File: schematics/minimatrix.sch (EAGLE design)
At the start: 9 parts

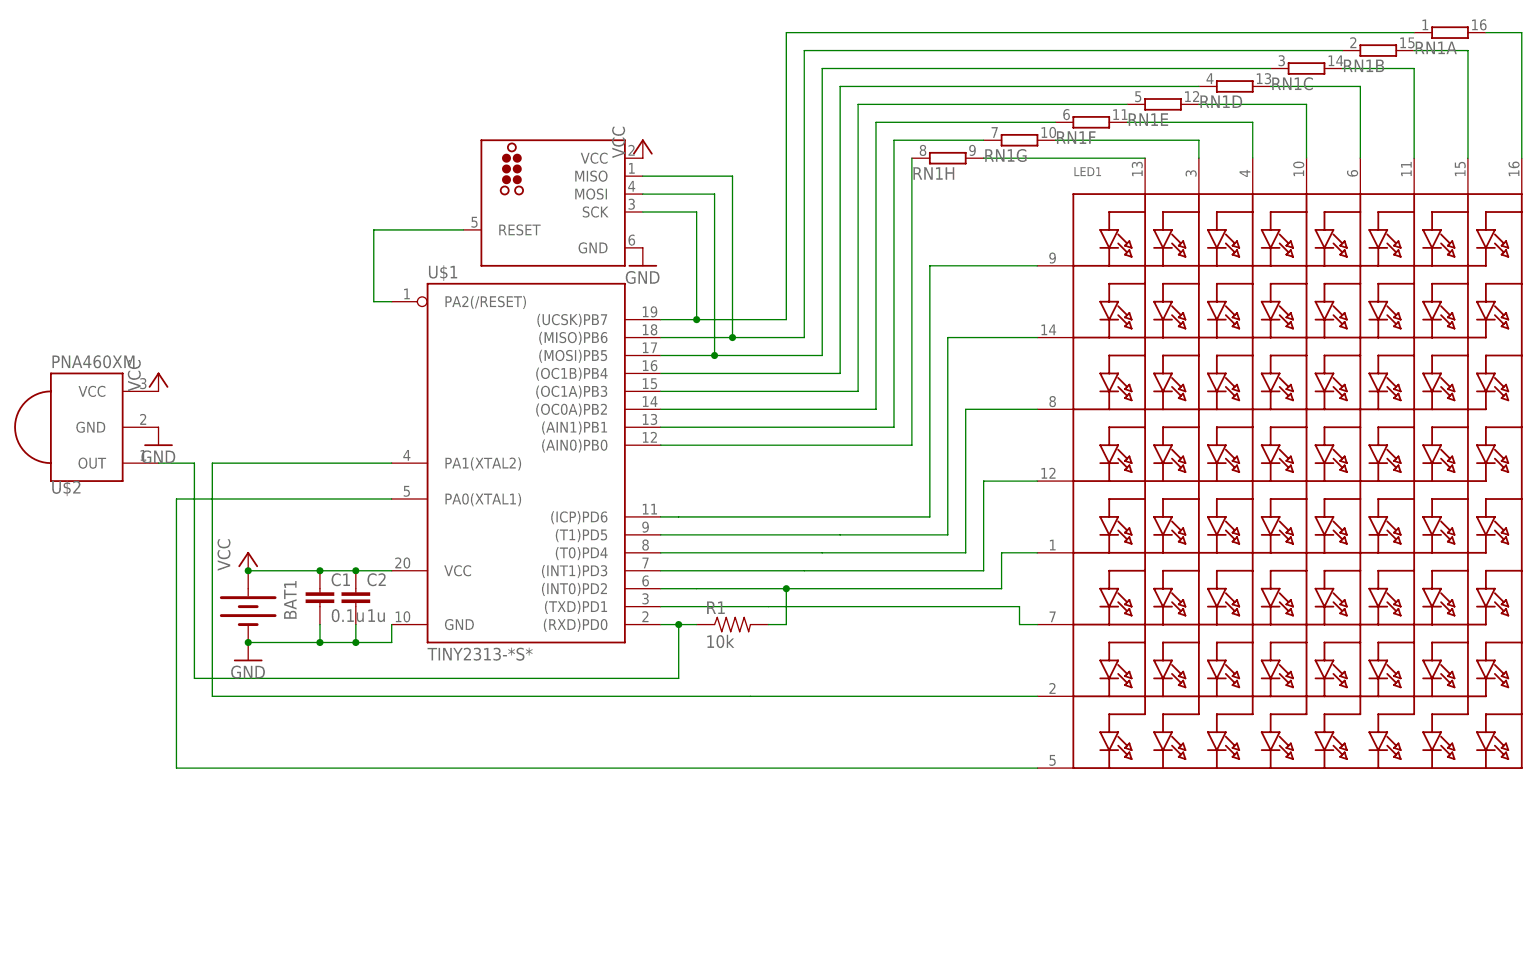
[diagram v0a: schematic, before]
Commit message: Update design restoring IR receiver.
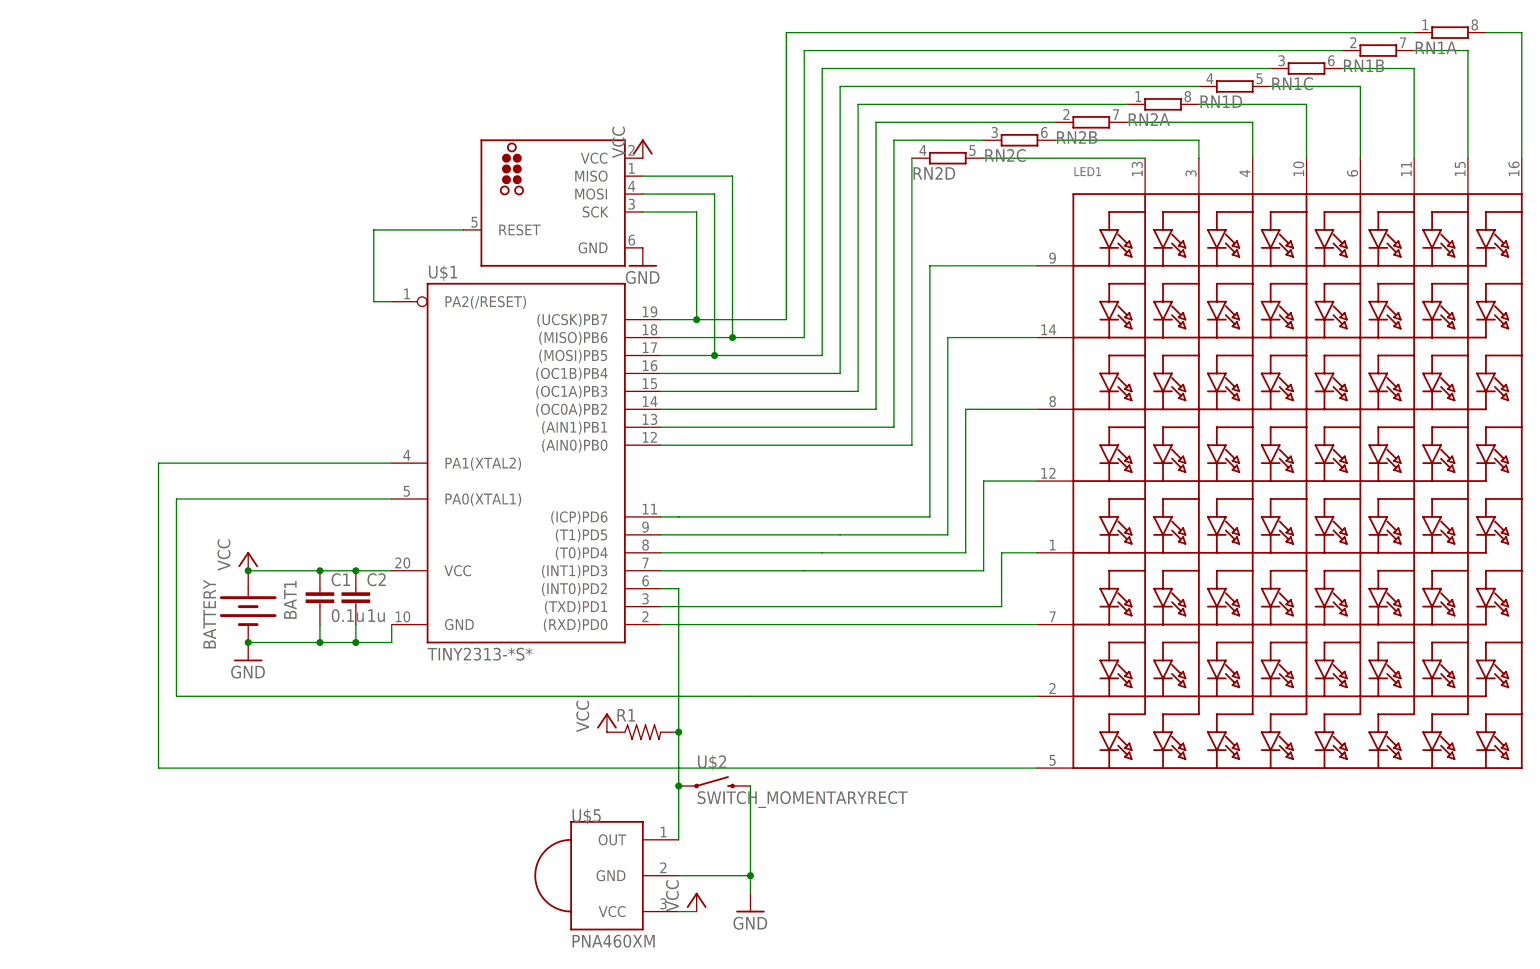
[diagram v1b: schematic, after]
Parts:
- added RN2: (no value), resistor-dil:4R-NCAY16
- added U$5: PNA460XM, adafruit:PNA460XM
- BAT1: value (none) -> BATTERY; device SparkFun-Electromechanical:BATTERY20MM_4LEGS -> nickparts:BATTERY
- R1: value 10k -> (none)
- RN1: device resistor-dil:8R-NEXB2HV -> resistor-dil:4R-NCAY16
- U$2: value PNA460XM -> SWITCH_MOMENTARYRECT; device adafruit:PNA460XM -> nickparts:SWITCH_MOMENTARYRECT
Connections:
- removed net R6: LED1.K6, U$1.(TXD)PD1
- removed net R8: LED1.K8, U$1.PA0(XTAL1)
- removed net ROW5: U$1.PA1(XTAL2)
- new net N$12: LED1.K8, U$1.PA1(XTAL2)
- new net N$13: R1.2, U$1.(INT0)PD2, U$2.1, U$5.OUT
- net C1: now also RN2D.1; no longer RN1H.1
- net C2: now also RN2C.1; no longer RN1G.1
- net C3: now also RN2B.1; no longer RN1F.1
- net C4: now also RN2A.1; no longer RN1E.1
- net GND: now also U$2.2, U$5.GND; no longer U$2.GND
- net N$1: now also LED1.K6; no longer R1.1, U$2.OUT
- net N$10: now also RN2D.2; no longer RN1H.2
- net N$11: now also U$1.(TXD)PD1; no longer R1.2, U$1.(INT0)PD2
- net N$3: now also RN2C.2; no longer RN1G.2
- net N$4: now also RN2B.2; no longer RN1F.2
- net N$5: now also RN2A.2; no longer RN1E.2
- net R7: now also U$1.PA0(XTAL1)
- net VCC: now also R1.1, U$5.VCC; no longer U$2.VCC
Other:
- moved on the sheet: R1, RN1A, RN1B, RN1C, RN1D

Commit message: Tweaks for production version
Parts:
- renumbered U$1 to IC1, U$2 to SW1, U$5 to IC2
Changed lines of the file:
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@@
 <parts>
 <part name="LED1" library="adafruit" deviceset="SEGMENT_8X8_ROWCATHODE" device="M12A881UR"/>
-<part name="U$1" library="avr-7" deviceset="TINY2313*" device="-*S*"/>
+<part name="IC1" library="avr-7" deviceset="TINY2313*" device="-*S*"/>
 <part name="BAT1" library="nickparts" deviceset="BATTERY" device=""/>
 <part name="U$3" library="tag-connect" deviceset="TC2030_AVR" device="MCP-NL"/>
@@
 <part name="RN1" library="resistor-dil" deviceset="4R-N" device="CAY16"/>
 <part name="RN2" library="resistor-dil" deviceset="4R-N" device="CAY16"/>
-<part name="U$2" library="nickparts" deviceset="SWITCH_MOMENTARY" device="RECT"/>
+<part name="SW1" library="nickparts" deviceset="SWITCH_MOMENTARY" device="RECT"/>
 <part name="GND3" library="supply1" deviceset="GND" device=""/>
-<part name="U$5" library="adafruit" deviceset="PNA460XM" device=""/>
+<part name="IC2" library="adafruit" deviceset="PNA460XM" device=""/>
 <part name="P+3" library="supply1" deviceset="VCC" device=""/>
 <part name="R1" library="SparkFun-Passives" deviceset="RESISTOR" device="0805-RES"/>
@@
 <instances>
 <instance part="LED1" gate="G$1" x="106.68" y="55.88"/>
-<instance part="U$1" gate="G$1" x="-2.54" y="66.04"/>
+<instance part="IC1" gate="G$1" x="-2.54" y="66.04"/>
 <instance part="BAT1" gate="G$1" x="-43.18" y="40.64" rot="R270"/>
 <instance part="U$3" gate="G$1" x="10.16" y="88.9" rot="MR0"/>
@@
 <instance part="RN2" gate="C" x="66.04" y="106.68"/>
 <instance part="RN2" gate="D" x="55.88" y="104.14"/>
-<instance part="U$2" gate="G$1" x="22.86" y="15.24"/>
+<instance part="SW1" gate="G$1" x="22.86" y="15.24"/>
 <instance part="GND3" gate="1" x="27.94" y="-2.54"/>
-<instance part="U$5" gate="G$1" x="7.62" y="2.54"/>
+<instance part="IC2" gate="G$1" x="7.62" y="2.54"/>
 <instance part="P+3" gate="VCC" x="20.32" y="0"/>
 <instance part="R1" gate="G$1" x="12.7" y="22.86"/>
@@
 <pinref part="BAT1" gate="G$1" pin="+"/>
 <pinref part="P+1" gate="VCC" pin="VCC"/>
-<pinref part="U$1" gate="G$1" pin="VCC"/>
+<pinref part="IC1" gate="G$1" pin="VCC"/>
 <wire x1="-22.86" y1="45.72" x2="-27.94" y2="45.72" width="0.1524" layer="91"/>
 <junction x="-43.18" y="45.72"/>
@@
 </segment>
 <segment>
-<pinref part="U$5" gate="G$1" pin="VCC"/>
+<pinref part="IC2" gate="G$1" pin="VCC"/>
 <pinref part="P+3" gate="VCC" pin="VCC"/>
 <wire x1="20.32" y1="-2.54" x2="17.78" y2="-2.54" width="0.1524" layer="91"/>
@@
 <pinref part="BAT1" gate="G$1" pin="-"/>
 <pinref part="GND2" gate="1" pin="GND"/>
-<pinref part="U$1" gate="G$1" pin="GND"/>
+<pinref part="IC1" gate="G$1" pin="GND"/>
 <wire x1="-43.18" y1="35.56" x2="-33.02" y2="35.56" width="0.1524" layer="91"/>
 <wire x1="-33.02" y1="35.56" x2="-27.94" y2="35.56" width="0.1524" layer="91"/>
@@
 </segment>
 <segment>
-<pinref part="U$2" gate="G$1" pin="2"/>
+<pinref part="SW1" gate="G$1" pin="2"/>
 <pinref part="GND3" gate="1" pin="GND"/>
 <wire x1="27.94" y1="15.24" x2="27.94" y2="2.54" width="0.1524" layer="91"/>
-<pinref part="U$5" gate="G$1" pin="GND"/>
+<pinref part="IC2" gate="G$1" pin="GND"/>
 <wire x1="27.94" y1="2.54" x2="27.94" y2="0" width="0.1524" layer="91"/>
 <wire x1="17.78" y1="2.54" x2="27.94" y2="2.54" width="0.1524" layer="91"/>
@@
 <net name="C8" class="0">
 <segment>
-<pinref part="U$1" gate="G$1" pin="(UCSK)PB7"/>
+<pinref part="IC1" gate="G$1" pin="(UCSK)PB7"/>
 <wire x1="15.24" y1="81.28" x2="20.32" y2="81.28" width="0.1524" layer="91"/>
 <wire x1="20.32" y1="81.28" x2="20.32" y2="96.52" width="0.1524" layer="91"/>
@@
 <net name="N$2" class="0">
 <segment>
-<pinref part="U$1" gate="G$1" pin="PA2(/RESET)"/>
+<pinref part="IC1" gate="G$1" pin="PA2(/RESET)"/>
 <wire x1="-22.86" y1="83.82" x2="-25.4" y2="83.82" width="0.1524" layer="91"/>
 <wire x1="-25.4" y1="83.82" x2="-25.4" y2="93.98" width="0.1524" layer="91"/>
@@
 <wire x1="12.7" y1="99.06" x2="22.86" y2="99.06" width="0.1524" layer="91"/>
 <wire x1="22.86" y1="99.06" x2="22.86" y2="76.2" width="0.1524" layer="91"/>
-<pinref part="U$1" gate="G$1" pin="(MOSI)PB5"/>
+<pinref part="IC1" gate="G$1" pin="(MOSI)PB5"/>
 <wire x1="22.86" y1="76.2" x2="15.24" y2="76.2" width="0.1524" layer="91"/>
 <wire x1="38.1" y1="116.84" x2="38.1" y2="76.2" width="0.1524" layer="91"/>
@@
 <wire x1="12.7" y1="101.6" x2="25.4" y2="101.6" width="0.1524" layer="91"/>
 <wire x1="25.4" y1="101.6" x2="25.4" y2="78.74" width="0.1524" layer="91"/>
-<pinref part="U$1" gate="G$1" pin="(MISO)PB6"/>
+<pinref part="IC1" gate="G$1" pin="(MISO)PB6"/>
 <wire x1="25.4" y1="78.74" x2="15.24" y2="78.74" width="0.1524" layer="91"/>
 <wire x1="35.56" y1="119.38" x2="35.56" y2="78.74" width="0.1524" layer="91"/>
@@
 <wire x1="53.34" y1="88.9" x2="68.58" y2="88.9" width="0.1524" layer="91"/>
 <wire x1="53.34" y1="53.34" x2="17.78" y2="53.34" width="0.1524" layer="91"/>
-<pinref part="U$1" gate="G$1" pin="(ICP)PD6"/>
+<pinref part="IC1" gate="G$1" pin="(ICP)PD6"/>
 <wire x1="17.78" y1="53.34" x2="15.24" y2="53.34" width="0.1524" layer="91"/>
 </segment>
@@
 <net name="R2" class="0">
 <segment>
-<pinref part="U$1" gate="G$1" pin="(T1)PD5"/>
+<pinref part="IC1" gate="G$1" pin="(T1)PD5"/>
 <wire x1="15.24" y1="50.8" x2="40.64" y2="50.8" width="0.1524" layer="91"/>
 <wire x1="55.88" y1="50.8" x2="55.88" y2="78.74" width="0.1524" layer="91"/>
@@
 <net name="R3" class="0">
 <segment>
-<pinref part="U$1" gate="G$1" pin="(T0)PD4"/>
+<pinref part="IC1" gate="G$1" pin="(T0)PD4"/>
 <wire x1="15.24" y1="48.26" x2="38.1" y2="48.26" width="0.1524" layer="91"/>
 <wire x1="58.42" y1="48.26" x2="58.42" y2="68.58" width="0.1524" layer="91"/>
@@
 <net name="R4" class="0">
 <segment>
-<pinref part="U$1" gate="G$1" pin="(INT1)PD3"/>
+<pinref part="IC1" gate="G$1" pin="(INT1)PD3"/>
 <wire x1="15.24" y1="45.72" x2="35.56" y2="45.72" width="0.1524" layer="91"/>
 <wire x1="60.96" y1="45.72" x2="60.96" y2="58.42" width="0.1524" layer="91"/>
@@
 <pinref part="LED1" gate="G$1" pin="K7"/>
 <wire x1="27.94" y1="27.94" x2="68.58" y2="27.94" width="0.1524" layer="91"/>
-<pinref part="U$1" gate="G$1" pin="PA0(XTAL1)"/>
+<pinref part="IC1" gate="G$1" pin="PA0(XTAL1)"/>
 <wire x1="-22.86" y1="55.88" x2="-53.34" y2="55.88" width="0.1524" layer="91"/>
 <wire x1="-53.34" y1="55.88" x2="-53.34" y2="27.94" width="0.1524" layer="91"/>
@@
 <segment>
 <wire x1="50.8" y1="104.14" x2="50.8" y2="63.5" width="0.1524" layer="91"/>
-<pinref part="U$1" gate="G$1" pin="(AIN0)PB0"/>
+<pinref part="IC1" gate="G$1" pin="(AIN0)PB0"/>
 <wire x1="50.8" y1="63.5" x2="15.24" y2="63.5" width="0.1524" layer="91"/>
 <pinref part="RN2" gate="D" pin="1"/>
@@
 <segment>
 <wire x1="48.26" y1="106.68" x2="48.26" y2="66.04" width="0.1524" layer="91"/>
-<pinref part="U$1" gate="G$1" pin="(AIN1)PB1"/>
+<pinref part="IC1" gate="G$1" pin="(AIN1)PB1"/>
 <wire x1="48.26" y1="66.04" x2="15.24" y2="66.04" width="0.1524" layer="91"/>
 <pinref part="RN2" gate="C" pin="1"/>
@@
 <segment>
 <wire x1="45.72" y1="109.22" x2="45.72" y2="68.58" width="0.1524" layer="91"/>
-<pinref part="U$1" gate="G$1" pin="(OC0A)PB2"/>
+<pinref part="IC1" gate="G$1" pin="(OC0A)PB2"/>
 <wire x1="45.72" y1="68.58" x2="15.24" y2="68.58" width="0.1524" layer="91"/>
 <pinref part="RN2" gate="B" pin="1"/>
@@
 <segment>
 <wire x1="43.18" y1="111.76" x2="43.18" y2="71.12" width="0.1524" layer="91"/>
-<pinref part="U$1" gate="G$1" pin="(OC1A)PB3"/>
+<pinref part="IC1" gate="G$1" pin="(OC1A)PB3"/>
 <wire x1="43.18" y1="71.12" x2="15.24" y2="71.12" width="0.1524" layer="91"/>
 <pinref part="RN2" gate="A" pin="1"/>
@@
 <segment>
 <wire x1="40.64" y1="114.3" x2="40.64" y2="73.66" width="0.1524" layer="91"/>
-<pinref part="U$1" gate="G$1" pin="(OC1B)PB4"/>
+<pinref part="IC1" gate="G$1" pin="(OC1B)PB4"/>
 <wire x1="40.64" y1="73.66" x2="15.24" y2="73.66" width="0.1524" layer="91"/>
 <pinref part="RN1" gate="D" pin="1"/>
@@
 <wire x1="63.5" y1="48.26" x2="68.58" y2="48.26" width="0.1524" layer="91"/>
 <wire x1="63.5" y1="48.26" x2="63.5" y2="40.64" width="0.1524" layer="91"/>
-<pinref part="U$1" gate="G$1" pin="(TXD)PD1"/>
+<pinref part="IC1" gate="G$1" pin="(TXD)PD1"/>
 <wire x1="63.5" y1="40.64" x2="15.24" y2="40.64" width="0.1524" layer="91"/>
 </segment>
@@
 <wire x1="68.58" y1="17.78" x2="-55.88" y2="17.78" width="0.1524" layer="91"/>
 <wire x1="-55.88" y1="17.78" x2="-55.88" y2="60.96" width="0.1524" layer="91"/>
-<pinref part="U$1" gate="G$1" pin="PA1(XTAL2)"/>
+<pinref part="IC1" gate="G$1" pin="PA1(XTAL2)"/>
 <wire x1="-55.88" y1="60.96" x2="-22.86" y2="60.96" width="0.1524" layer="91"/>
 </segment>
@@
 <net name="N$1" class="0">
 <segment>
-<pinref part="U$1" gate="G$1" pin="(RXD)PD0"/>
+<pinref part="IC1" gate="G$1" pin="(RXD)PD0"/>
 <pinref part="LED1" gate="G$1" pin="K6"/>
 <wire x1="15.24" y1="38.1" x2="68.58" y2="38.1" width="0.1524" layer="91"/>
@@
 <net name="N$13" class="0">
 <segment>
-<pinref part="U$1" gate="G$1" pin="(INT0)PD2"/>
-<pinref part="U$2" gate="G$1" pin="1"/>
+<pinref part="IC1" gate="G$1" pin="(INT0)PD2"/>
+<pinref part="SW1" gate="G$1" pin="1"/>
 <wire x1="15.24" y1="43.18" x2="17.78" y2="43.18" width="0.1524" layer="91"/>
 <wire x1="17.78" y1="43.18" x2="17.78" y2="22.86" width="0.1524" layer="91"/>
-<pinref part="U$5" gate="G$1" pin="OUT"/>
+<pinref part="IC2" gate="G$1" pin="OUT"/>
 <wire x1="17.78" y1="22.86" x2="17.78" y2="15.24" width="0.1524" layer="91"/>
 <wire x1="17.78" y1="15.24" x2="17.78" y2="7.62" width="0.1524" layer="91"/>

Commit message: Numerous changes and improvements
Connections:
- net C1 renamed COL1
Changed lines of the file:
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@@
 <?xml version="1.0" encoding="utf-8"?>
 <!DOCTYPE eagle SYSTEM "eagle.dtd">
-<eagle version="6.2">
+<eagle version="6.4">
 <drawing>
 <settings>
@@
 </segment>
 </net>
-<net name="C1" class="0">
+<net name="COL1" class="0">
 <segment>
 <wire x1="50.8" y1="104.14" x2="50.8" y2="63.5" width="0.1524" layer="91"/>

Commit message: Work on programmer code; don't accept commands when asleep
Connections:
- net C6 renamed MOSI
- net C7 renamed MISO
- net C8 renamed SCK
- net N$2 renamed RESET
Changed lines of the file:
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@@
 </segment>
 </net>
-<net name="C8" class="0">
+<net name="SCK" class="0">
 <segment>
 <pinref part="IC1" gate="G$1" pin="(UCSK)PB7"/>
@@
 </segment>
 </net>
-<net name="N$2" class="0">
+<net name="RESET" class="0">
 <segment>
 <pinref part="IC1" gate="G$1" pin="PA2(/RESET)"/>
@@
 </segment>
 </net>
-<net name="C6" class="0">
+<net name="MOSI" class="0">
 <segment>
 <pinref part="U$3" gate="G$1" pin="MOSI"/>
@@
 </segment>
 </net>
-<net name="C7" class="0">
+<net name="MISO" class="0">
 <segment>
 <pinref part="U$3" gate="G$1" pin="MISO"/>
